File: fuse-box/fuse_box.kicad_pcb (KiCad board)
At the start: 2 copper layers, 70 x 50 mm, 46 parts, among them J1 PWR, J3 Conn_02x05_Counter_Clockwise, U1 AP63200WU

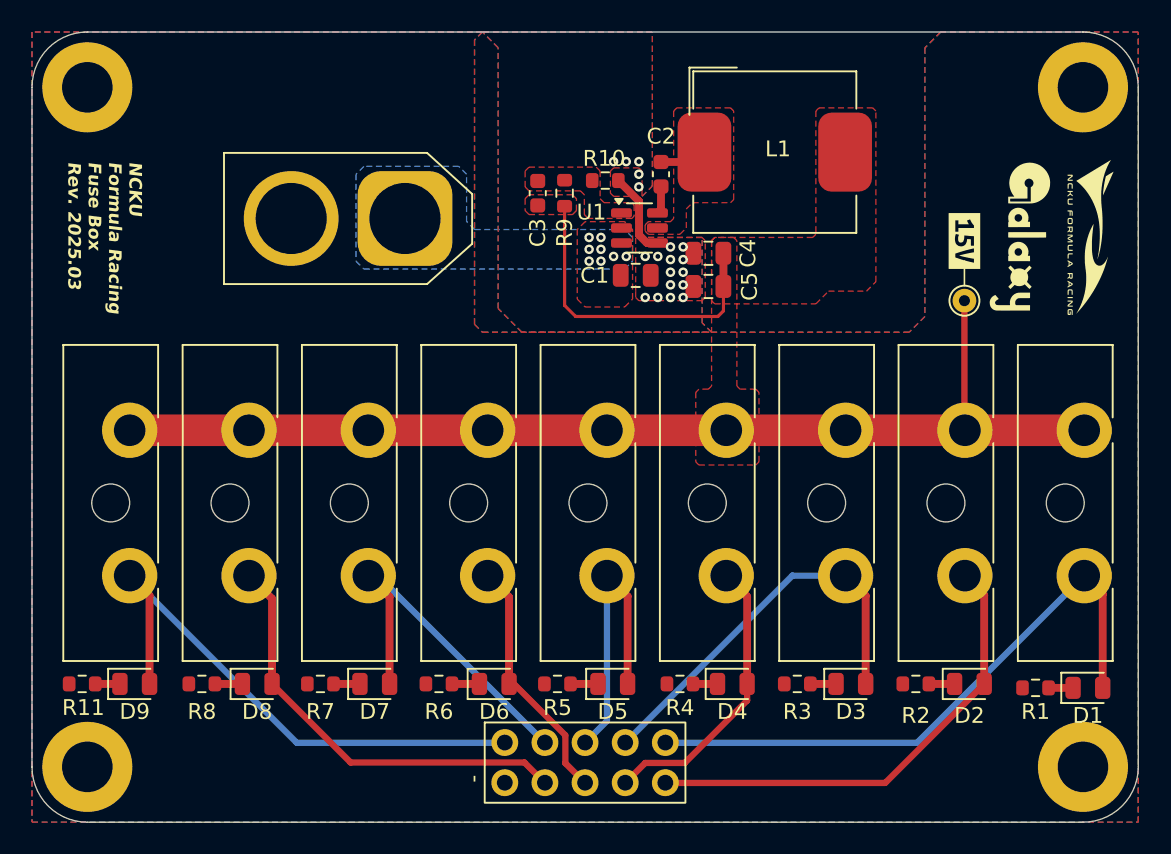
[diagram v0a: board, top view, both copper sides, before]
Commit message: feat: improve buck feedback
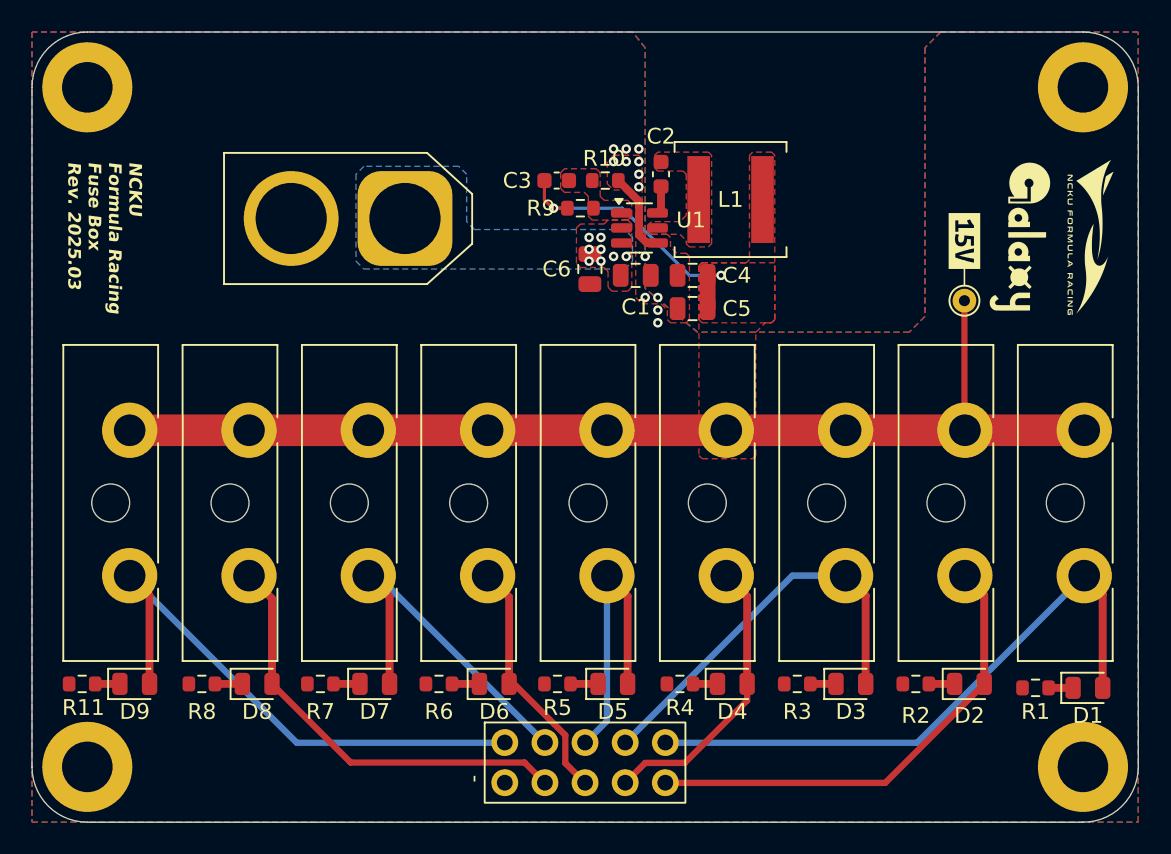
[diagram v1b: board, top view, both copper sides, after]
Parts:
- added C6: 10u, Capacitor_SMD:C_0805_2012Metric, F.Cu at (100.1, 51.6)
- L1: footprint Inductor_SMD:L_Bourns_SRP1050WA -> Inductor_SMD:L_Coilcraft_XAL6060-XXX
- moved L1 4.10 mm to (109.0, 47.2)
- moved C4 1.72 mm to (106.6, 52.0)
- moved C5 1.72 mm to (106.6, 54.1)
- moved C3 1.44 mm to (98.0, 46.0), turned to 0 degrees
- moved R9 1.38 mm to (99.5, 47.8), turned to 0 degrees
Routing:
- net Net-(U1-SW): track 3.01 -> 0.00 mm
- net +15V: track 89.0 -> 86.8 mm, vias 0 -> 2
- net GND: vias 19 -> 13

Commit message: Add files via upload
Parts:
- F1, F2, F3, F4, F5, F6, F7, F8, F9: value 10A -> 178.6164.0001; footprint PCM_Fuse_AKL:Fuseholder_Blade_ATO_Littelfuse_Pudenz_2_Pin -> fuseholder:LITTELFUSE_178.6164.0001
- moved F1 4.75 mm to (130.2, 66.4)
- moved F3 4.75 mm to (115.1, 66.4)
- moved F4 4.75 mm to (107.5, 66.4)
- moved F5 4.75 mm to (100.0, 66.4)
- moved F8 4.75 mm to (77.3, 66.4)
- moved F9 4.75 mm to (69.8, 66.4)
- moved F2 4.75 mm to (122.7, 66.4)
- moved F6 4.75 mm to (92.5, 66.4)
- moved F7 4.75 mm to (84.9, 66.4)
- moved kibuzzard-67D51968 0.62 mm to (123.8, 49.2)
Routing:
- net +15V: track 86.8 -> 110.4 mm

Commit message: v2025.10
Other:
- board text added: "NCKU Formula Racing Fuse Box Rev. 2025.10"
- board text removed: "NCKU Formula Racing Fuse Box Rev. 2025.03"
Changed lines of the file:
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@@
   (gr_arc (start 68.3 86.6) (mid 65.825126 85.574874) (end 64.8 83.1)
     (stroke (width 0.05) (type default)) (layer "Edge.Cuts"))
-  (gr_text "NCKU\nFormula Racing\nFuse Box\nRev. 2025.03" (at 67 44.8 270) (layer "F.SilkS")
+  (gr_text "NCKU\nFormula Racing\nFuse Box\nRev. 2025.10" (at 67 44.8 270) (layer "F.SilkS")
     (effects (font (size 0.8 0.8) (thickness 0.15) bold italic) (justify left bottom))
   )
